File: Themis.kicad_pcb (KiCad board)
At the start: 2 copper layers, 100 x 50 mm, 515 parts, among them J10 Conn_01x01, J11 Conn_01x01, J12 Conn_01x01, J13 Conn_01x01, J17 SMA, J18 Conn_01x01, J20 Conn_01x01, J5 Conn_01x05, J7 SMA, J8 SMA, T1 Tr 1/33, T2 Tr 33/1, U1 LMC6482

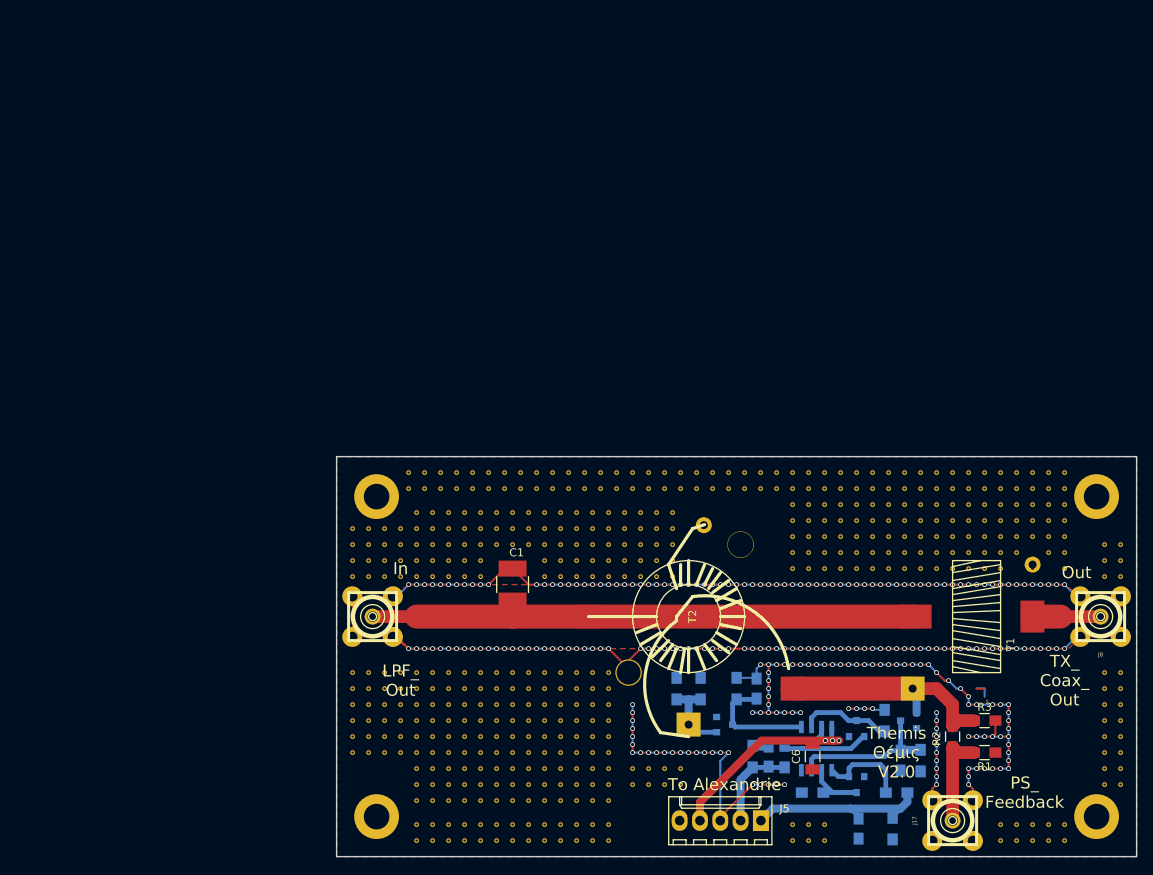
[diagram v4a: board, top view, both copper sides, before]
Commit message: Attenuator and RF Pure signal out on lower side
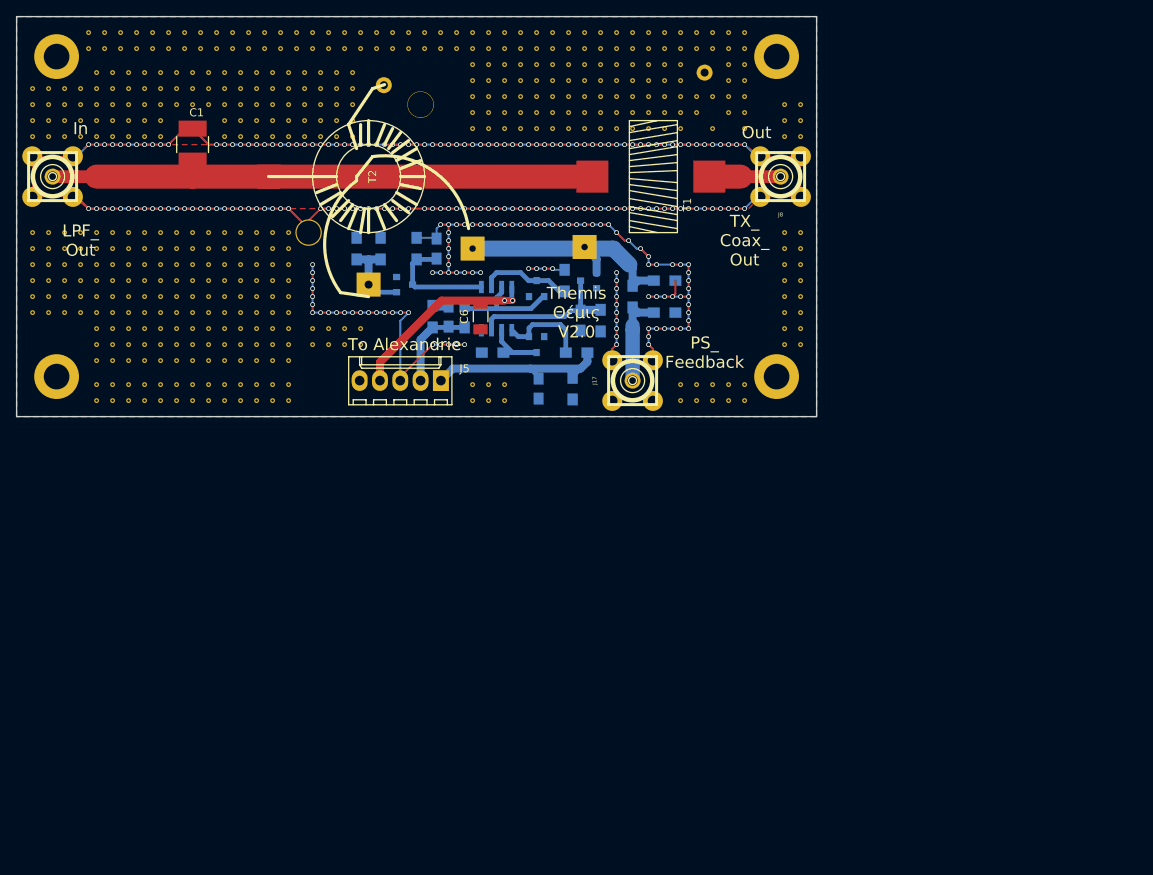
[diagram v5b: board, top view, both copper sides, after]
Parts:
- removed the REF** at (177.0, 91.0)
- removed the REF** at (175.0, 93.0)
- removed the REF** at (177.0, 93.0)
- removed the REF** at (175.0, 91.0)
- R1, R2, R3: moved to B.Cu
- moved C6 68.9 mm to (108.0, 67.5)
- moved T1 68.2 mm to (129.6, 50.0)
- moved C1 68.0 mm to (72.0, 46.0)
- moved C2 68.0 mm to (115.2, 76.5)
- moved C3 68.0 mm to (120.5, 68.0)
- moved C4 68.0 mm to (102.5, 59.0)
- moved C5 68.0 mm to (104.0, 67.5)
- moved D1 68.0 mm to (121.5, 63.0)
- moved D2 68.0 mm to (115.0, 71.0)
- moved D3 68.0 mm to (98.5, 63.5)
- moved D4 68.0 mm to (115.0, 64.0)
- moved J10 68.0 mm to (55.0, 75.0)
- moved J11 68.0 mm to (145.0, 75.0)
- moved J12 68.0 mm to (55.0, 35.0)
- moved J13 68.0 mm to (145.0, 35.0)
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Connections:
- J5 pad 5: Net-(J5-Pad5) -> (no net)
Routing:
- net Net-(D1-Pad2): track 29.7 -> 37.1 mm
- net (no net): track 3.05 -> 0.00 mm
- net Net-(D4-Pad2): track 14.8 -> 13.7 mm
- net Net-(J17-Pad1): track 12.1 -> 13.0 mm
- net +12V: track 28.1 -> 28.0 mm, vias 3 -> 2
